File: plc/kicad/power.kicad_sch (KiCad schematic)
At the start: 73 parts, among them Q5 BSS138LT1G, Q6 CSD19537Q3, SW3 TSD003B08026A03, U15 TPS54560BDDAR, U16 TPS26630RGER, U17 TPS7A5201QRGRRQ1, U21 BZT52C3V3S

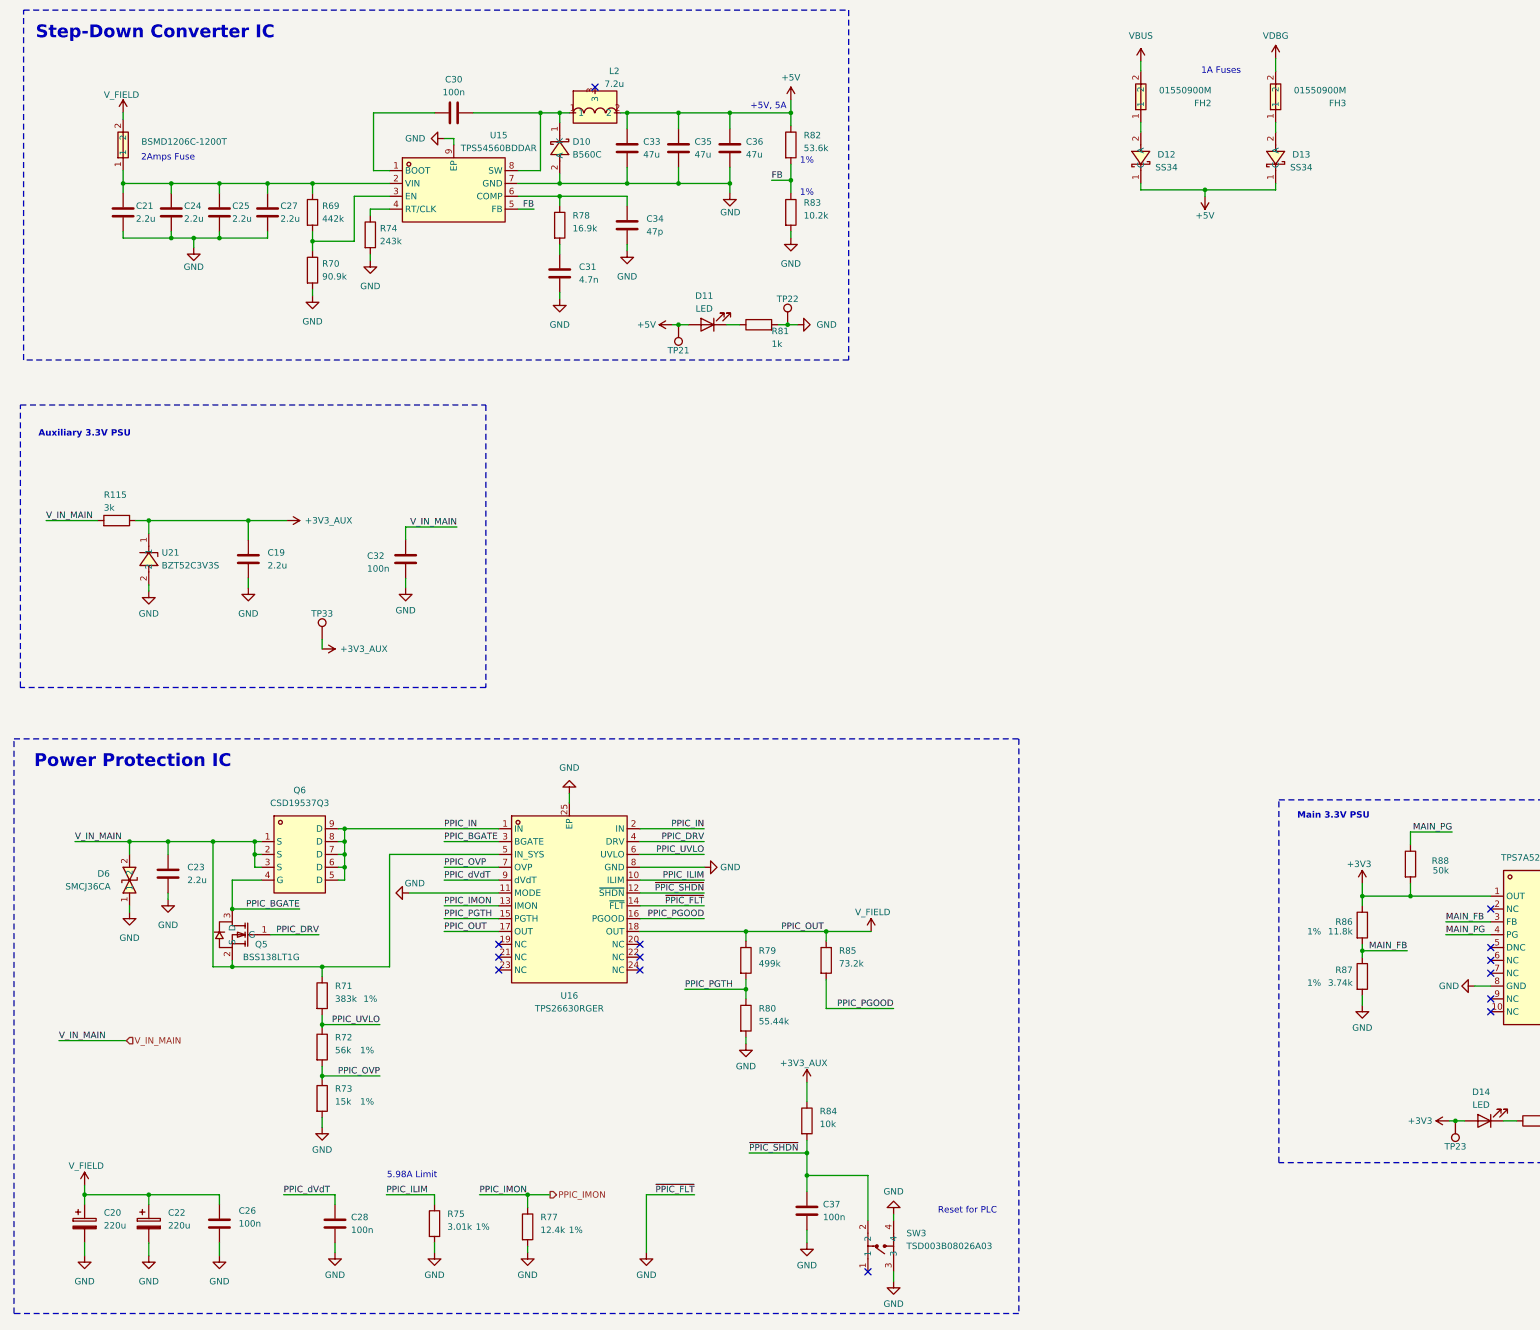
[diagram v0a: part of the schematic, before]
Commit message: BOM Consolidation
- CP2102N Vdbg divider: 22.1k→5.1k, 47.5k→10k (gives 3.29V)
- I²C pull-ups (R65,R66): 4.7k→5.1k (verified ok)
- Buck UVLO (R69,R70): 442k→100k, 90.9k→2×10k (UVLO = 7V)
- TPS272C45D ILIM (R75): 3k→3×10k (~6A limit)
- PPIC IMON + ETH_EXPRESS (R77,R100): 12.4k→2×6.2k
- Buck compensation (R78): 16.9k→10k+6.2k+620 series
- PPIC PGTH divider (R79,R80): 499k→100k, 55.44k→2×10k (PGTH = 7.2V)
- Buck feedback (R82,R83): 53.6k→52.5k 1%, 10.2k→10k 1%
- 3.3V LDO power-good (R88): 50k→100k

| Metric                 | Before | After | Change             |
| ---------------------- | ------ | ----- | ------------------ |
| Unique resistor values | 33     | 22    | **−11 (−33%)**     |
| Total resistor count   | 110    | 118   | +8 (series splits) |
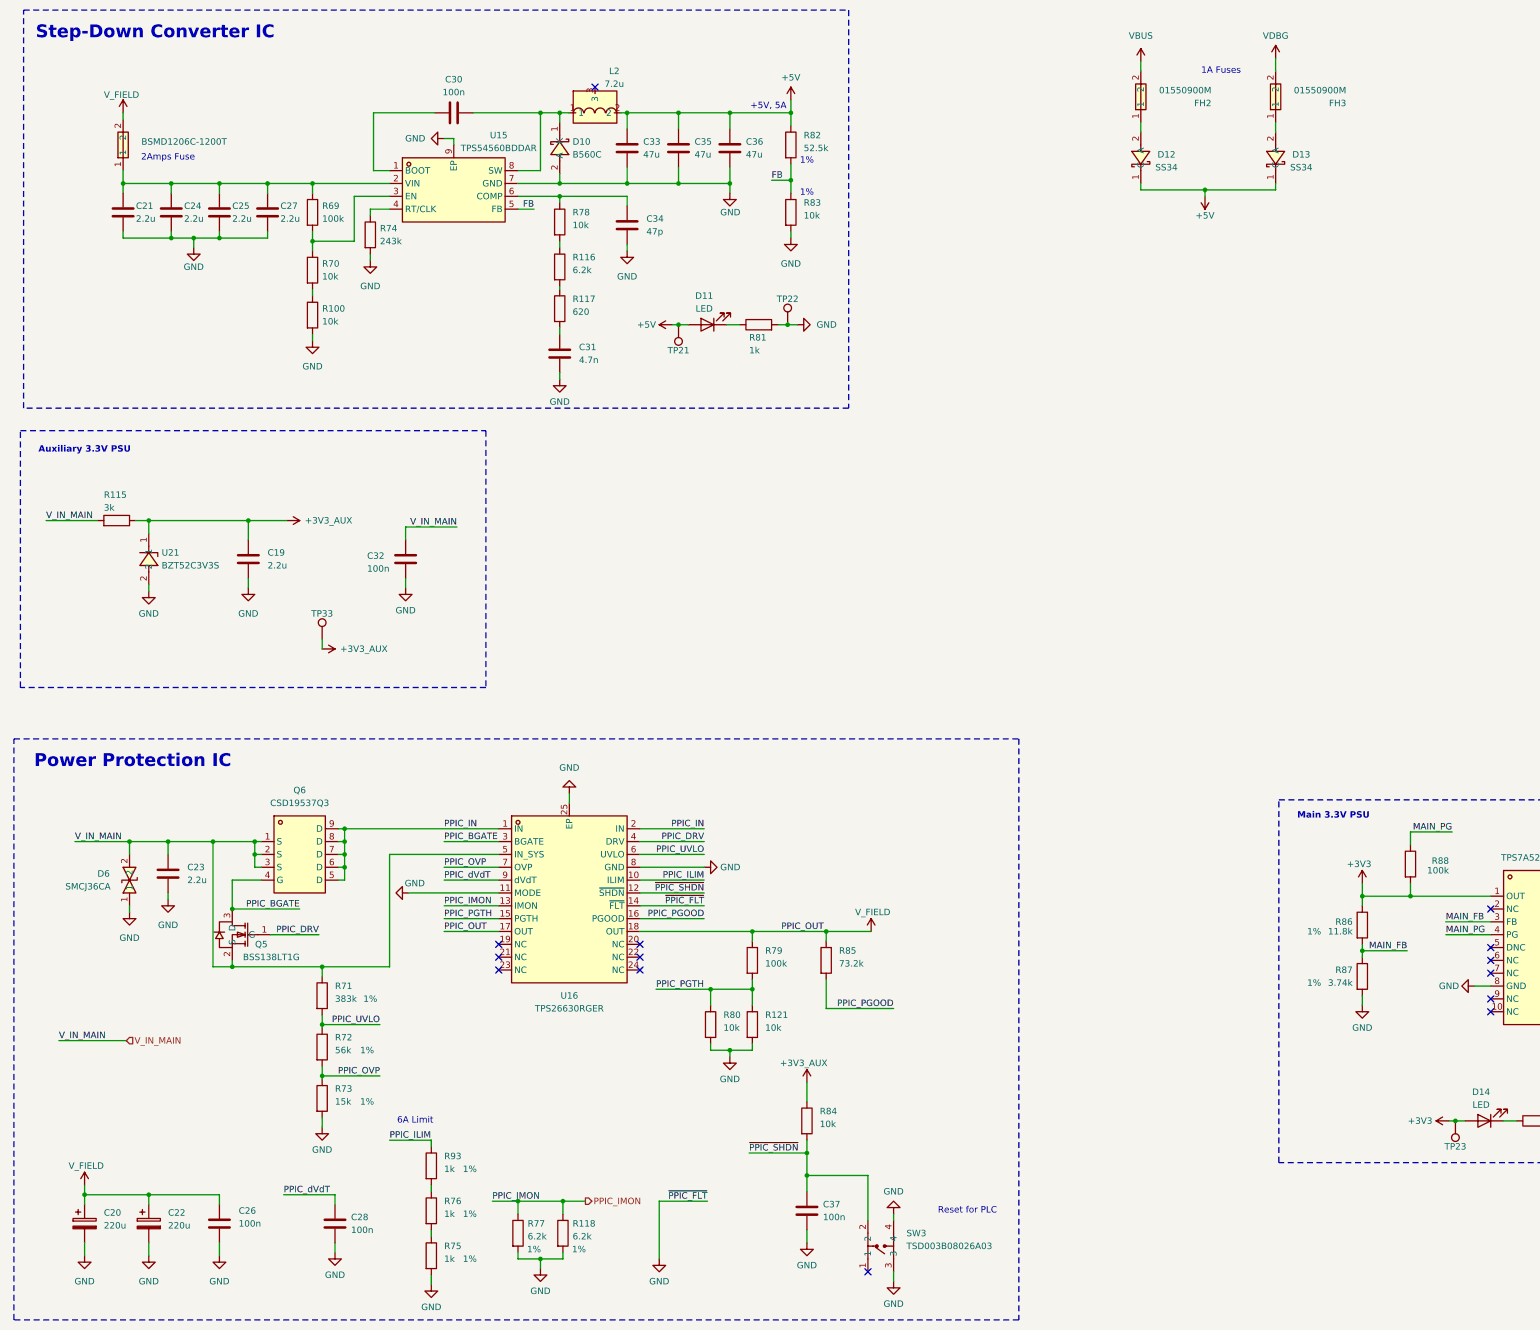
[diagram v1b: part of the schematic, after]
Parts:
- added R100, R121: 10k, Resistor_SMD:R_0603_1608Metric, symbol Device:R
- added R116, R118: 6.2k, Resistor_SMD:R_0603_1608Metric, symbol Device:R
- added R117: 620, Resistor_SMD:R_0603_1608Metric, symbol Device:R
- added R76, R93: 1k, Resistor_SMD:R_0603_1608Metric, symbol Device:R
- R69: value 442k -> 100k
- R70: value 90.9k -> 10k
- R75: value 3.01k -> 1k
- R77: value 12.4k -> 6.2k
- R78: value 16.9k -> 10k
- R79: value 499k -> 100k
- R80: value 55.44k -> 10k
- R82: value 53.6k -> 52.5k
- R83: value 10.2k -> 10k
- R88: value 50k -> 100k
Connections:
- net GND: now also R100.2, R118.2, R121.2; no longer R70.2
- net PPIC_ILIM: now also R93.1; no longer R75.1
- net PPIC_IMON: now also R118.1
- net PPIC_PGTH: now also R121.1
- net at R78.2: now also R116.1; no longer C31.2
- new net: R75.1, R76.2
- new net: R116.2, R117.1
- new net: C31.2, R117.2
- new net: R100.1, R70.2
- new net: R76.1, R93.2
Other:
- note added: "6A Limit"
- note removed: "5.98A Limit"
- moved on the sheet: C31, R75, R77, R78, R79, R80

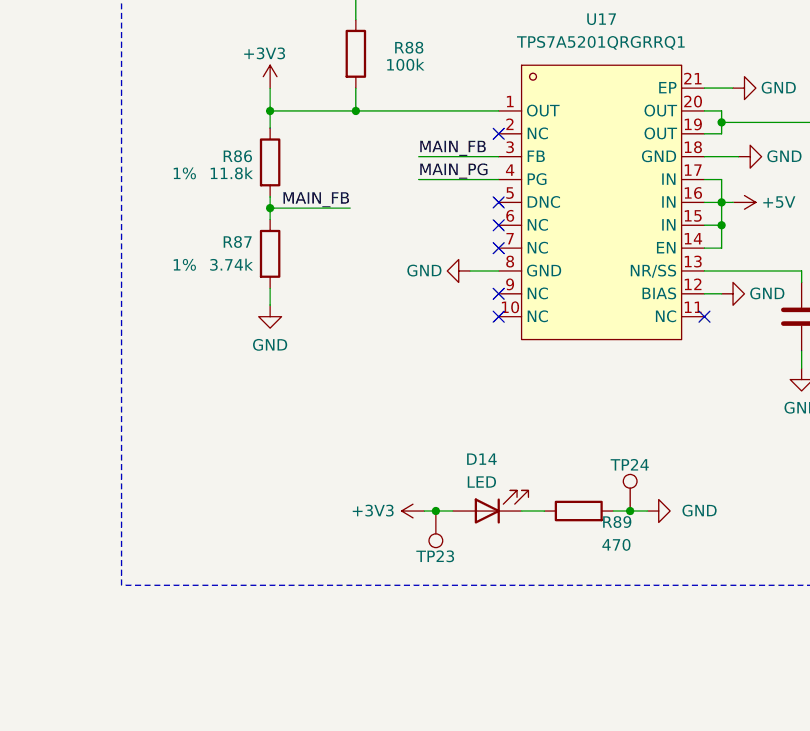
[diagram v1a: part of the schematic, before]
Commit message: BOM consolidation
Consolidated two more resistor values
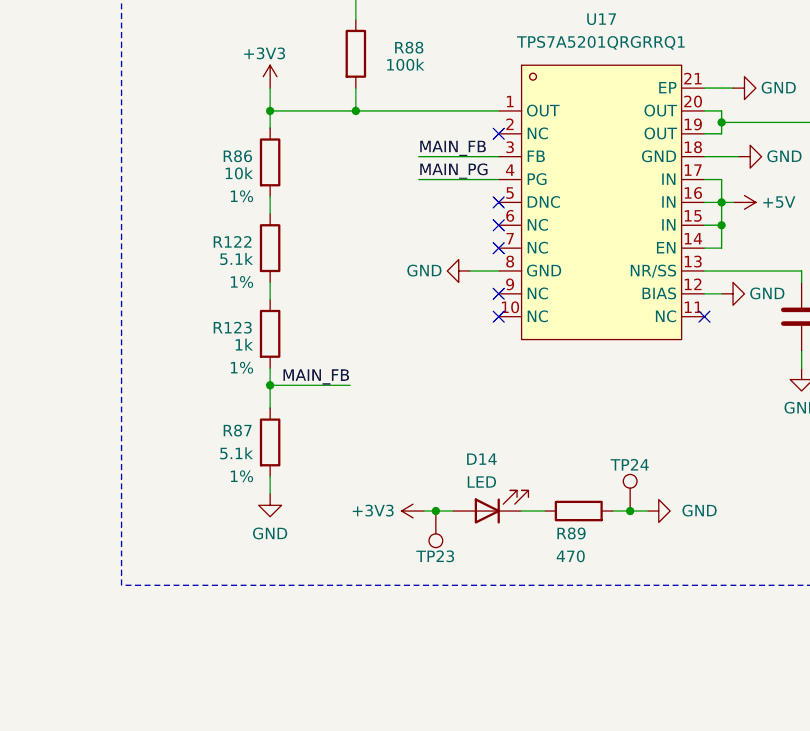
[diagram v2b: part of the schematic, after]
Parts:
- added R122: 5.1k, Resistor_SMD:R_0603_1608Metric, symbol Device:R
- added R123: 1k, Resistor_SMD:R_0603_1608Metric, symbol Device:R
- R86: value 11.8k -> 10k
- R87: value 3.74k -> 5.1k
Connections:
- net MAIN_FB: now also R123.2; no longer R86.2
- new net: R122.1, R86.2
- new net: R122.2, R123.1
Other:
- moved on the sheet: R87
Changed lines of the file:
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@@
 	)
 	(junction
+		(at 287.02 225.425)
+		(diameter 0)
+		(color 0 0 0 0)
+	)
+	(junction
 		(at 124.46 40.005)
 		(diameter 0)
@@
 	)
 	(junction
-		(at 287.02 205.74)
-		(diameter 0)
-		(color 0 0 0 0)
-	)
-	(junction
 		(at 59.69 184.15)
 		(diameter 0)
@@
 	(wire
 		(pts
-			(xy 295.91 205.74) (xy 287.02 205.74)
+			(xy 295.91 225.425) (xy 287.02 225.425)
+		)
+		(stroke
+			(width 0)
+			(type default)
+		)
+	)
+	(wire
+		(pts
+			(xy 287.02 206.375) (xy 287.02 204.47)
 		)
 		(stroke
@@
 	(wire
 		(pts
+			(xy 287.02 223.52) (xy 287.02 225.425)
+		)
+		(stroke
+			(width 0)
+			(type default)
+		)
+	)
+	(wire
+		(pts
 			(xy 85.725 181.61) (xy 85.725 184.15)
 		)
@@
 	(wire
 		(pts
+			(xy 287.02 215.9) (xy 287.02 213.995)
+		)
+		(stroke
+			(width 0)
+			(type default)
+		)
+	)
+	(wire
+		(pts
 			(xy 303.53 200.025) (xy 312.42 200.025)
 		)
@@
 	(wire
 		(pts
-			(xy 287.02 204.47) (xy 287.02 205.74)
-		)
-		(stroke
-			(width 0)
-			(type default)
-		)
-	)
-	(wire
-		(pts
 			(xy 105.41 184.15) (xy 116.205 184.15)
 		)
@@
 	(wire
 		(pts
-			(xy 287.02 216.535) (xy 287.02 214.63)
+			(xy 287.02 237.49) (xy 287.02 235.585)
 		)
 		(stroke
@@
 	(wire
 		(pts
+			(xy 287.02 225.425) (xy 287.02 227.965)
+		)
+		(stroke
+			(width 0)
+			(type default)
+		)
+	)
+	(wire
+		(pts
 			(xy 177.165 250.19) (xy 189.23 250.19)
 		)
@@
 	(wire
 		(pts
-			(xy 287.02 205.74) (xy 287.02 207.01)
-		)
-		(stroke
-			(width 0)
-			(type default)
-		)
-	)
-	(wire
-		(pts
 			(xy 347.98 96.52) (xy 347.98 99.695)
 		)
@@
 	)
 	(label "MAIN_FB"
-		(at 295.91 205.74 180)
+		(at 295.91 225.425 180)
 		(effects
 			(font
@@
 	(symbol
 		(lib_id "Device:R")
-		(at 287.02 210.82 0)
+		(at 287.02 231.775 0)
 		(unit 1)
 		(body_style 1)
@@
 		(dnp no)
 		(property "Reference" "R87"
-			(at 285.115 209.55 0)
+			(at 285.115 230.505 0)
 			(show_name no)
 			(do_not_autoplace no)
@@
 			)
 		)
-		(property "Value" "3.74k"
-			(at 285.115 212.09 0)
+		(property "Value" "5.1k"
+			(at 285.115 233.045 0)
 			(show_name no)
 			(do_not_autoplace no)
@@
 		)
 		(property "Footprint" "Resistor_SMD:R_0603_1608Metric"
-			(at 285.242 210.82 90)
+			(at 285.242 231.775 90)
 			(hide yes)
 			(show_name no)
@@
 		)
 		(property "Datasheet" ""
-			(at 287.02 210.82 0)
+			(at 287.02 231.775 0)
 			(hide yes)
 			(show_name no)
@@
 		)
 		(property "Description" "Resistor"
-			(at 287.02 210.82 0)
+			(at 287.02 231.775 0)
 			(hide yes)
 			(show_name no)
@@
 		)
 		(property "Tolerance" "1%"
-			(at 277.495 212.09 0)
+			(at 283.845 235.585 0)
 			(show_name no)
 			(do_not_autoplace no)
@@
 			)
 		)
-		(property "Value" "11.8k"
+		(property "Value" "10k"
 			(at 285.115 201.93 0)
 			(show_name no)
@@
 		)
 		(property "Tolerance" "1%"
-			(at 277.495 201.93 0)
+			(at 283.845 204.47 0)
 			(show_name no)
 			(do_not_autoplace no)
@@
 	)
 	(symbol
+		(lib_id "Device:R")
+		(at 287.02 210.185 0)
+		(unit 1)
+		(body_style 1)
+		(exclude_from_sim no)
+		(in_bom yes)
+		(on_board yes)
+		(in_pos_files yes)
+		(dnp no)
+		(property "Reference" "R122"
+			(at 285.115 209.55 0)
+			(show_name no)
+			(do_not_autoplace no)
+			(effects
+				(font
+					(size 1.27 1.27)
+				)
+				(justify right)
+			)
+		)
+		(property "Value" "5.1k"
+			(at 285.115 211.455 0)
+			(show_name no)
+			(do_not_autoplace no)
+			(effects
+				(font
+					(size 1.27 1.27)
+				)
+				(justify right)
+			)
+		)
+		(property "Footprint" "Resistor_SMD:R_0603_1608Metric"
+			(at 285.242 210.185 90)
+			(hide yes)
+			(show_name no)
+			(do_not_autoplace no)
+			(effects
+				(font
+					(size 1.27 1.27)
+				)
+			)
+		)
+		(property "Datasheet" ""
+			(at 287.02 210.185 0)
+			(hide yes)
+			(show_name no)
+			(do_not_autoplace no)
+			(effects
+				(font
+					(size 1.27 1.27)
+				)
+			)
+		)
+		(property "Description" "Resistor"
+			(at 287.02 210.185 0)
+			(hide yes)
+			(show_name no)
+			(do_not_autoplace no)
+			(effects
+				(font
+					(size 1.27 1.27)
+				)
+			)
+		)
+		(property "Tolerance" "1%"
+			(at 283.845 213.995 0)
+			(show_name no)
+			(do_not_autoplace no)
+			(effects
+				(font
+					(size 1.27 1.27)
+				)
+			)
+		)
+		(pin "2"
+		)
+		(pin "1"
+		)
+		(instances
+			(project "LibrePLC32"
+				(path "/ef4c1a27-85a3-413a-9f93-a41c4f97eee5/7cb27fd0-1c73-4e87-ad2d-fb4e463ee9fb"
+					(reference "R122")
+					(unit 1)
+				)
+			)
+		)
+	)
+	(symbol
 		(lib_id "power:GND")
 		(at 328.93 239.395 90)
@@
 	(symbol
 		(lib_id "power:GND")
-		(at 287.02 216.535 0)
+		(at 287.02 237.49 0)
 		(mirror y)
 		(unit 1)
@@
 		(dnp no)
 		(property "Reference" "#PWR0181"
-			(at 287.02 222.885 0)
+			(at 287.02 243.84 0)
 			(hide yes)
 			(show_name no)
@@
 		)
 		(property "Value" "GND"
-			(at 287.02 220.98 0)
+			(at 287.02 241.935 0)
 			(show_name no)
 			(do_not_autoplace no)
@@
 		)
 		(property "Footprint" ""
-			(at 287.02 216.535 0)
+			(at 287.02 237.49 0)
 			(hide yes)
 			(show_name no)
@@
 		)
 		(property "Datasheet" ""
-			(at 287.02 216.535 0)
+			(at 287.02 237.49 0)
 			(hide yes)
 			(show_name no)
@@
 		)
 		(property "Description" "Power symbol creates a global label with name \"GND\" , ground"
-			(at 287.02 216.535 0)
+			(at 287.02 237.49 0)
 			(hide yes)
 			(show_name no)
@@
 		(dnp no)
 		(property "Reference" "R89"
-			(at 323.85 240.665 90)
+			(at 318.77 241.935 90)
 			(show_name no)
 			(do_not_autoplace no)
@@
 		)
 		(property "Value" "470"
-			(at 323.85 243.205 90)
+			(at 318.77 244.475 90)
 			(show_name no)
 			(do_not_autoplace no)
@@
 					(unit 1)
 				)
+			)
+		)
+	)
+	(symbol
+		(lib_id "Device:R")
+		(at 287.02 219.71 0)
+		(unit 1)
+		(body_style 1)
+		(exclude_from_sim no)
+		(in_bom yes)
+		(on_board yes)
+		(in_pos_files yes)
+		(dnp no)
+		(property "Reference" "R123"
+			(at 285.115 219.075 0)
+			(show_name no)
+			(do_not_autoplace no)
+			(effects
+				(font
+					(size 1.27 1.27)
+				)
+				(justify right)
+			)
+		)
+		(property "Value" "1k"
+			(at 285.115 220.98 0)
+			(show_name no)
+			(do_not_autoplace no)
+			(effects
+				(font
+					(size 1.27 1.27)
+				)
+				(justify right)
+			)
+		)
+		(property "Footprint" "Resistor_SMD:R_0603_1608Metric"
+			(at 285.242 219.71 90)
+			(hide yes)
+			(show_name no)
+			(do_not_autoplace no)
+			(effects
+				(font
+					(size 1.27 1.27)
+				)
+			)
+		)
+		(property "Datasheet" ""
+			(at 287.02 219.71 0)
+			(hide yes)
+			(show_name no)
+			(do_not_autoplace no)
+			(effects
+				(font
+					(size 1.27 1.27)
+				)
+			)
+		)
+		(property "Description" "Resistor"
+			(at 287.02 219.71 0)
+			(hide yes)
+			(show_name no)
+			(do_not_autoplace no)
+			(effects
+				(font
+					(size 1.27 1.27)
+				)
+			)
+		)
+		(property "Tolerance" "1%"
+			(at 283.845 223.52 0)
+			(show_name no)
+			(do_not_autoplace no)
+			(effects
+				(font
+					(size 1.27 1.27)
+				)
+			)
+		)
+		(pin "2"
+		)
+		(pin "1"
+		)
+		(instances
+			(project "LibrePLC32"
+				(path "/ef4c1a27-85a3-413a-9f93-a41c4f97eee5/7cb27fd0-1c73-4e87-ad2d-fb4e463ee9fb"
+					(reference "R123")
+					(unit 1)
+				)

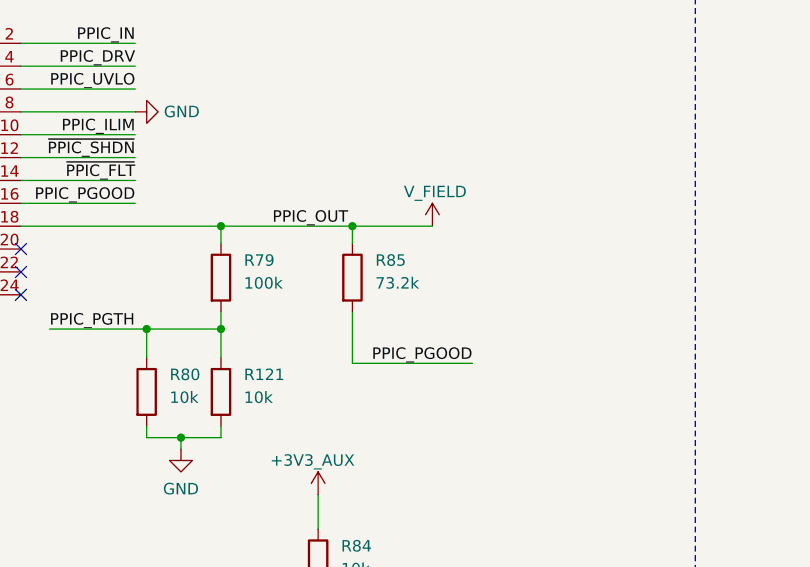
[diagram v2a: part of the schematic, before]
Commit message: Modified PPIC_PGOOD to 100k
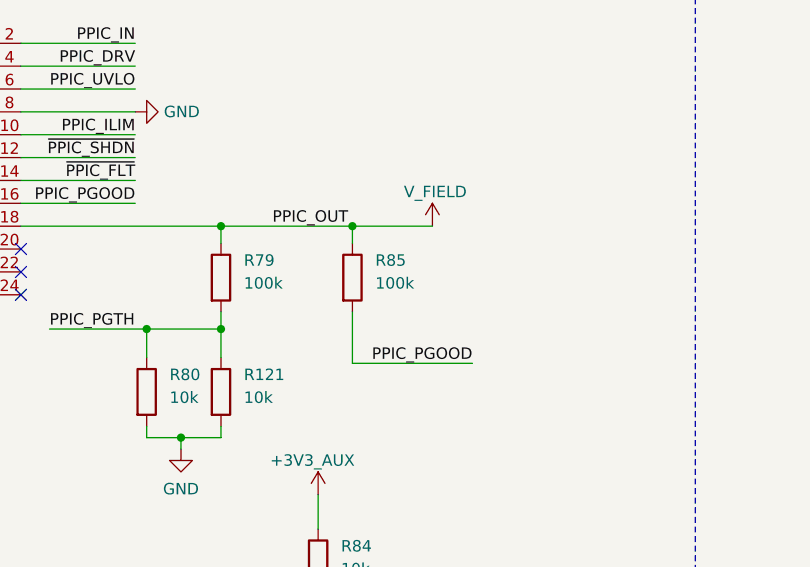
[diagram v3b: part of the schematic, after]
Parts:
- R85: value 73.2k -> 100k
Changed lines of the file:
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@@
 			)
 		)
-		(property "Value" "73.2k"
+		(property "Value" "100k"
 			(at 183.515 208.28 0)
 			(show_name no)
